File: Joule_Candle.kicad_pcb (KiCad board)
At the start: 2 copper layers, 14 x 80 mm, 7 parts, among them Q1 BC817-40

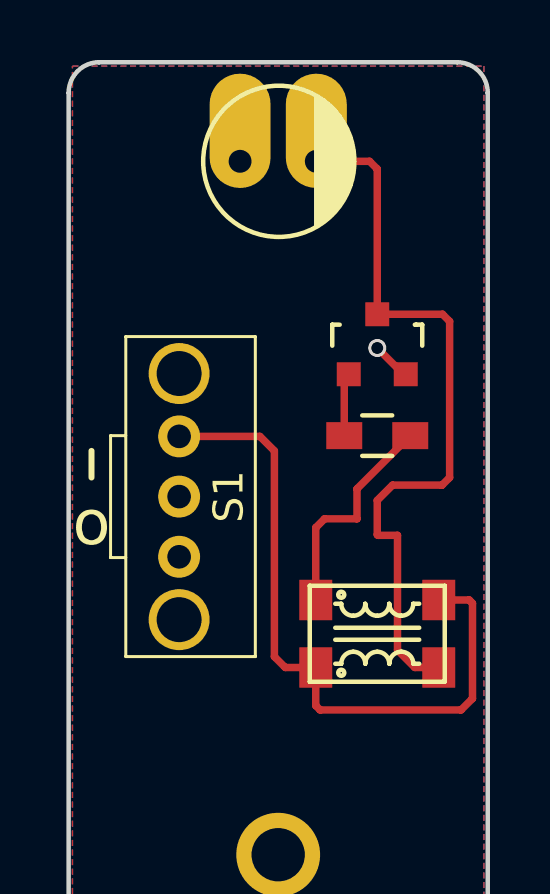
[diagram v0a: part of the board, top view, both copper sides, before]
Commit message: change LED footprint
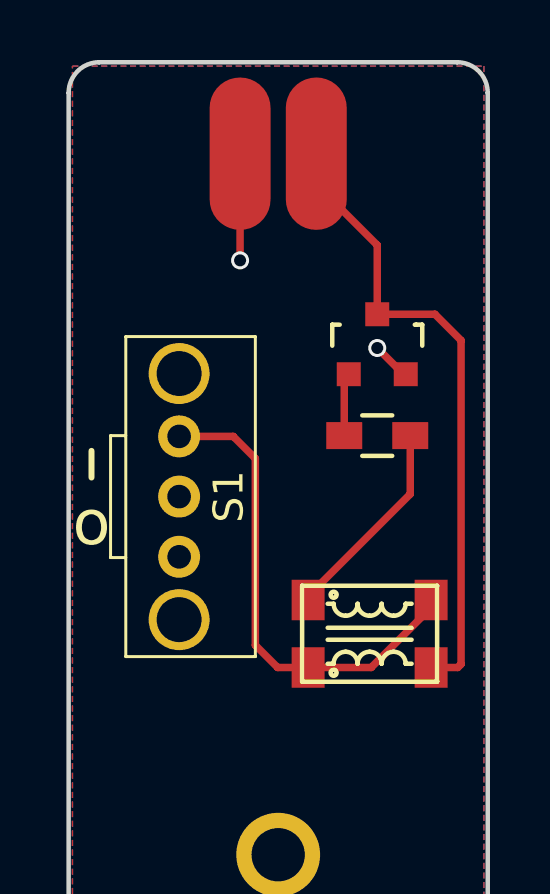
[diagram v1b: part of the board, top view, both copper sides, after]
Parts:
- D1: footprint LEDs:3mm_PCB_Edge -> lib_fp:3mm_PCB_Edge
- moved D1 0.76 mm to (162.3, 55.9)
- moved L1 0.25 mm to (164.1, 70.9)
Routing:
- net Net-(L1-Pad1): track 22.8 -> 16.2 mm
- net Net-(D1-Pad2): track 24.7 -> 20.2 mm
- net GND: track 1.31 -> 3.85 mm, vias 1 -> 2
- net Net-(L1-Pad4): track 7.42 -> 6.89 mm
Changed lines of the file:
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@@
     (thickness 1.6)
     (drawings 61)
-    (tracks 37)
+    (tracks 24)
     (zones 0)
     (modules 7)
@@
       (net 2 GND))
   )
-  (module LEDs:3mm_PCB_Edge (layer F.Cu)
-    (at 162.306 55.118)
-    (fp_text reference D1 (at -1.27 3.302) (layer F.SilkS) hide
-      (effects (font (size 1 1) (thickness 0.15)))
-    )
-    (fp_text value LED (at -1.143 1.397) (layer F.Fab)
-      (effects (font (size 1 1) (thickness 0.15)))
-    )
-    (fp_line (start 1.143 0.762) (end 1.143 -0.762) (layer F.SilkS) (width 0.15))
-    (fp_line (start 1.016 -1.016) (end 1.016 1.016) (layer F.SilkS) (width 0.15))
-    (fp_line (start 0.889 1.27) (end 0.889 -1.27) (layer F.SilkS) (width 0.15))
-    (fp_line (start 0.762 -1.524) (end 0.762 1.397) (layer F.SilkS) (width 0.15))
-    (fp_line (start 0.635 1.651) (end 0.635 -1.651) (layer F.SilkS) (width 0.15))
-    (fp_line (start 0.508 -1.778) (end 0.508 1.778) (layer F.SilkS) (width 0.15))
-    (fp_line (start 0.381 1.905) (end 0.381 -1.905) (layer F.SilkS) (width 0.15))
-    (fp_line (start 0.254 -2.032) (end 0.254 1.905) (layer F.SilkS) (width 0.15))
-    (fp_line (start 0.127 2.032) (end 0.127 -2.032) (layer F.SilkS) (width 0.15))
-    (fp_line (start 0 2.159) (end 0 -2.159) (layer F.SilkS) (width 0.15))
-    (fp_circle (center -1.25 0) (end 1.27 0) (layer F.SilkS) (width 0.15))
-    (pad 1 thru_hole oval (at -2.54 0) (size 2.032 3.81) (drill 0.762 (offset 0 -1.016)) (layers *.Cu *.Mask F.SilkS)
-      (net 2 GND))
-    (pad 2 thru_hole oval (at 0 0) (size 2.032 3.81) (drill 0.762 (offset 0 -1.016)) (layers *.Cu *.Mask F.SilkS)
-      (net 3 "Net-(D1-Pad2)"))
-    (model "../../../../../../home/sam/Dropbox/FreeCAD/Joule Thief/3mmLED.wrl"
-      (at (xyz -0.05 0 0))
-      (scale (xyz 0.3937 0.3937 0.3937))
-      (rotate (xyz 0 0 0))
-    )
-  )
   (module TO_SOT_Packages_SMD:SOT-23 (layer F.Cu)
     (at 164.338 61.214)
@@
   )
   (module Inductor:SRF4532-510Y (layer F.Cu)
-    (at 164.338 70.866)
+    (at 164.084 70.866)
     (fp_text reference L1 (at 0 2.6) (layer F.SilkS) hide
       (effects (font (size 1 1) (thickness 0.15)))
@@
       (xy 2.975 8.625)) (layer F.SilkS) (width 0.01))
   )
+  (module lib_fp:3mm_PCB_Edge (layer F.Cu)
+    (at 162.306 55.88)
+    (fp_text reference D1 (at 0 0) (layer F.SilkS) hide
+      (effects (font (size 1 1) (thickness 0.15)))
+    )
+    (fp_text value LED (at -1.143 1.397) (layer F.Fab)
+      (effects (font (size 1 1) (thickness 0.15)))
+    )
+    (pad 1 smd oval (at -2.54 0) (size 2.032 5.08) (drill (offset 0 -1.016)) (layers F.Cu F.Paste F.Mask)
+      (net 2 GND))
+    (pad 2 smd oval (at 0 0) (size 2.032 5.08) (drill (offset 0 -1.016)) (layers F.Cu F.Paste F.Mask)
+      (net 3 "Net-(D1-Pad2)"))
+    (model "../../../../../../home/sam/Dropbox/FreeCAD/Joule Thief/3mmLED.wrl"
+      (at (xyz -0.05 0 0))
+      (scale (xyz 0.3937 0.3937 0.3937))
+      (rotate (xyz 0 0 0))
+    )
+  )
   (gr_line (start 156.972 126.746) (end 165.1 126.746) (angle 90) (layer B.SilkS) (width 0.2))
   (gr_arc (start 165.1 126.111) (end 165.1 125.476) (angle 90) (layer B.SilkS) (width 0.2))
@@
   (gr_arc (start 167.005 52.832) (end 167.005 51.816) (angle 90) (layer Edge.Cuts) (width 0.15))
   (gr_line (start 154.051 131.826) (end 168.021 131.826) (angle 90) (layer Edge.Cuts) (width 0.15))
+  (segment (start 159.766 55.88) (end 159.766 58.42) (width 0.25) (layer F.Cu) (net 2) (status 400000))
+  (via (at 159.766 58.42) (size 0.6) (drill 0.4) (layers F.Cu B.Cu) (net 2))
   (segment (start 165.288 62.21476) (end 165.21176 62.21476) (width 0.25) (layer F.Cu) (net 2))
   (segment (start 165.21176 62.21476) (end 164.338 61.341) (width 0.25) (layer F.Cu) (net 2))
   (via (at 164.338 61.341) (size 0.6) (drill 0.4) (layers F.Cu B.Cu) (net 2))
-  (segment (start 165.013 67.585) (end 164.359 67.585) (width 0.25) (layer F.Cu) (net 3))
-  (segment (start 166.51478 60.21578) (end 164.338 60.21578) (width 0.25) (layer F.Cu) (net 3))
-  (segment (start 166.751 60.452) (end 166.51478 60.21578) (width 0.25) (layer F.Cu) (net 3))
-  (segment (start 166.751 65.659) (end 166.751 60.452) (width 0.25) (layer F.Cu) (net 3))
-  (segment (start 166.497 65.913) (end 166.751 65.659) (width 0.25) (layer F.Cu) (net 3))
-  (segment (start 164.846 65.913) (end 166.497 65.913) (width 0.25) (layer F.Cu) (net 3))
-  (segment (start 164.338 66.421) (end 164.846 65.913) (width 0.25) (layer F.Cu) (net 3))
-  (segment (start 164.338 67.564) (end 164.338 66.421) (width 0.25) (layer F.Cu) (net 3))
-  (segment (start 164.359 67.585) (end 164.338 67.564) (width 0.25) (layer F.Cu) (net 3))
-  (segment (start 164.338 60.21578) (end 164.338 55.372) (width 0.25) (layer F.Cu) (net 3))
-  (segment (start 164.338 55.372) (end 164.084 55.118) (width 0.25) (layer F.Cu) (net 3))
-  (segment (start 164.084 55.118) (end 162.306 55.118) (width 0.25) (layer F.Cu) (net 3))
-  (segment (start 166.388 71.991) (end 165.59 71.991) (width 0.25) (layer F.Cu) (net 3))
-  (segment (start 165.013 71.414) (end 165.013 67.585) (width 0.25) (layer F.Cu) (net 3))
-  (segment (start 165.59 71.991) (end 165.013 71.414) (width 0.25) (layer F.Cu) (net 3))
-  (segment (start 162.288 71.991) (end 162.288 73.261) (width 0.25) (layer F.Cu) (net 4))
-  (segment (start 167.404 69.741) (end 166.388 69.741) (width 0.25) (layer F.Cu) (net 4))
-  (segment (start 167.513 69.85) (end 167.404 69.741) (width 0.25) (layer F.Cu) (net 4))
-  (segment (start 167.513 73.025) (end 167.513 69.85) (width 0.25) (layer F.Cu) (net 4))
-  (segment (start 167.132 73.406) (end 167.513 73.025) (width 0.25) (layer F.Cu) (net 4))
-  (segment (start 162.433 73.406) (end 167.132 73.406) (width 0.25) (layer F.Cu) (net 4))
-  (segment (start 162.288 73.261) (end 162.433 73.406) (width 0.25) (layer F.Cu) (net 4))
-  (segment (start 157.734 64.2874) (end 160.4264 64.2874) (width 0.25) (layer F.Cu) (net 4))
-  (segment (start 161.272 71.991) (end 162.288 71.991) (width 0.25) (layer F.Cu) (net 4))
-  (segment (start 160.909 71.628) (end 161.272 71.991) (width 0.25) (layer F.Cu) (net 4))
-  (segment (start 160.909 64.77) (end 160.909 71.628) (width 0.25) (layer F.Cu) (net 4))
-  (segment (start 160.4264 64.2874) (end 160.909 64.77) (width 0.25) (layer F.Cu) (net 4))
+  (segment (start 166.134 71.991) (end 167.023 71.991) (width 0.25) (layer F.Cu) (net 3) (status 400000))
+  (segment (start 166.26078 60.21578) (end 164.338 60.21578) (width 0.25) (layer F.Cu) (net 3) (status 800000))
+  (segment (start 167.132 61.087) (end 166.26078 60.21578) (width 0.25) (layer F.Cu) (net 3))
+  (segment (start 167.132 71.882) (end 167.132 61.087) (width 0.25) (layer F.Cu) (net 3))
+  (segment (start 167.023 71.991) (end 167.132 71.882) (width 0.25) (layer F.Cu) (net 3))
+  (segment (start 164.338 60.21578) (end 164.338 57.912) (width 0.25) (layer F.Cu) (net 3))
+  (segment (start 164.338 57.912) (end 162.306 55.88) (width 0.25) (layer F.Cu) (net 3))
+  (segment (start 157.734 64.2874) (end 159.5374 64.2874) (width 0.25) (layer F.Cu) (net 4) (status 400000))
+  (segment (start 161.018 71.991) (end 162.034 71.991) (width 0.25) (layer F.Cu) (net 4) (status 800000))
+  (segment (start 160.274 71.247) (end 161.018 71.991) (width 0.25) (layer F.Cu) (net 4))
+  (segment (start 160.274 65.024) (end 160.274 71.247) (width 0.25) (layer F.Cu) (net 4))
+  (segment (start 159.5374 64.2874) (end 160.274 65.024) (width 0.25) (layer F.Cu) (net 4))
+  (segment (start 162.288 71.991) (end 164.138 71.991) (width 0.25) (layer F.Cu) (net 4))
+  (segment (start 164.138 71.991) (end 166.388 69.741) (width 0.25) (layer F.Cu) (net 4))
   (segment (start 163.238 64.262) (end 163.238 62.36476) (width 0.25) (layer F.Cu) (net 6))
   (segment (start 163.238 62.36476) (end 163.388 62.21476) (width 0.25) (layer F.Cu) (net 6))
-  (segment (start 163.663 67.035) (end 163.663 66.037) (width 0.25) (layer F.Cu) (net 7))
-  (segment (start 163.663 66.037) (end 165.438 64.262) (width 0.25) (layer F.Cu) (net 7))
-  (segment (start 162.288 69.741) (end 162.288 67.328) (width 0.25) (layer F.Cu) (net 7))
-  (segment (start 162.581 67.035) (end 163.663 67.035) (width 0.25) (layer F.Cu) (net 7))
-  (segment (start 162.288 67.328) (end 162.581 67.035) (width 0.25) (layer F.Cu) (net 7))
+  (segment (start 162.034 69.741) (end 162.034 69.614) (width 0.25) (layer F.Cu) (net 7) (status C00000))
+  (segment (start 162.034 69.614) (end 165.438 66.21) (width 0.25) (layer F.Cu) (net 7) (status 400000))
+  (segment (start 165.438 66.21) (end 165.438 64.262) (width 0.25) (layer F.Cu) (net 7) (status 800000))
   (zone (net 2) (net_name GND) (layer B.Cu) (hatch edge 0.508)
     (connect_pads (clearance 0.508))

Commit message: remove 3d shapes
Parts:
- moved LOGO 2.07 mm to (159.8, 91.4)
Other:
- board text added: "Joule Thief Candle V2"
- board text added: "Sam Perry October 2017"
- board text removed: "Joule Thief Candle"
- board text removed: "Sam Perry November 2016"
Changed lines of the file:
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@@
     (links 11)
     (no_connects 0)
-    (area 152.949 51.740999 170.323715 131.901001)
+    (area 153.975999 51.740999 168.096001 131.901001)
     (thickness 1.6)
-    (drawings 61)
+    (drawings 36)
     (tracks 24)
     (zones 0)
@@
     (36 B.SilkS user)
     (37 F.SilkS user)
-    (38 B.Mask user hide)
-    (39 F.Mask user hide)
+    (38 B.Mask user)
+    (39 F.Mask user)
     (40 Dwgs.User user hide)
     (41 Cmts.User user hide)
@@
     (43 Eco2.User user hide)
     (44 Edge.Cuts user)
-    (45 Margin user hide)
+    (45 Margin user)
     (46 B.CrtYd user hide)
     (47 F.CrtYd user hide)
@@
     (pad 3 smd rect (at 0 -0.99822) (size 0.8001 0.8001) (layers F.Cu F.Paste F.Mask)
       (net 3 "Net-(D1-Pad2)"))
-    (model TO_SOT_Packages_SMD.3dshapes/SOT-23.wrl
-      (at (xyz 0 0 0))
-      (scale (xyz 1 1 1))
-      (rotate (xyz 0 0 0))
-    )
   )
   (module Resistors_SMD:R_0603_HandSoldering (layer F.Cu)
@@
     (pad 2 smd rect (at 1.1 0 180) (size 1.2 0.9) (layers F.Cu F.Paste F.Mask)
       (net 6 "Net-(Q1-Pad1)"))
-    (model Resistors_SMD.3dshapes/R_0603_HandSoldering.wrl
-      (at (xyz 0 0 0))
-      (scale (xyz 1 1 1))
-      (rotate (xyz 0 0 0))
-    )
   )
   (module Switches:SPDT_OS102011MA1QN1 (layer F.Cu)
@@
     (pad "" thru_hole circle (at -4.1021 0 90) (size 2.032 2.032) (drill 1.4986) (layers *.Cu *.Mask F.SilkS))
     (pad "" thru_hole circle (at 4.1021 0 90) (size 2.032 2.032) (drill 1.4986) (layers *.Cu *.Mask F.SilkS))
-    (model "../../../../../../home/sam/Dropbox/FreeCAD/AVR Dragon Shield/SPDT_Switch.wrl"
-      (at (xyz 0 0 0))
-      (scale (xyz 0.393701 0.393701 0.393701))
-      (rotate (xyz 0 0 180))
-    )
   )
   (module Inductor:SRF4532-510Y (layer F.Cu)
@@
   )
   (module Logo:P-Logo_Small (layer F.Cu)
-    (at 157.734 91.821)
+    (at 159.766 91.44)
     (fp_text reference LOGO (at 0 5) (layer F.SilkS) hide
       (effects (font (thickness 0.3)))
@@
     (pad 2 smd oval (at 0 0) (size 2.032 5.08) (drill (offset 0 -1.016)) (layers F.Cu F.Paste F.Mask)
       (net 3 "Net-(D1-Pad2)"))
-    (model "../../../../../../home/sam/Dropbox/FreeCAD/Joule Thief/3mmLED.wrl"
-      (at (xyz -0.05 0 0))
-      (scale (xyz 0.3937 0.3937 0.3937))
-      (rotate (xyz 0 0 0))
-    )
   )
-  (gr_line (start 156.972 126.746) (end 165.1 126.746) (angle 90) (layer B.SilkS) (width 0.2))
-  (gr_arc (start 165.1 126.111) (end 165.1 125.476) (angle 90) (layer B.SilkS) (width 0.2))
-  (gr_arc (start 156.972 126.111) (end 156.972 126.746) (angle 90) (layer B.SilkS) (width 0.2))
-  (gr_arc (start 165.1 126.111) (end 165.735 126.111) (angle 90) (layer B.SilkS) (width 0.2))
-  (gr_arc (start 156.972 126.111) (end 156.337 126.111) (angle 90) (layer B.SilkS) (width 0.2))
-  (gr_line (start 159.258 130.429) (end 159.639 127.254) (angle 90) (layer B.SilkS) (width 0.2))
-  (gr_line (start 162.814 130.429) (end 162.433 127.254) (angle 90) (layer B.SilkS) (width 0.2))
-  (gr_arc (start 163.195 130.429) (end 163.195 130.81) (angle 90) (layer B.SilkS) (width 0.2))
-  (gr_arc (start 158.877 130.429) (end 159.258 130.429) (angle 90) (layer B.SilkS) (width 0.2))
-  (gr_line (start 155.067 130.937) (end 155.067 131.191) (angle 90) (layer B.SilkS) (width 0.2))
-  (gr_line (start 167.005 130.937) (end 167.005 131.191) (angle 90) (layer B.SilkS) (width 0.2))
-  (gr_line (start 166.878 130.81) (end 155.194 130.81) (angle 90) (layer B.SilkS) (width 0.2))
-  (gr_arc (start 166.878 130.937) (end 166.878 130.81) (angle 90) (layer B.SilkS) (width 0.2))
-  (gr_arc (start 155.194 130.937) (end 155.067 130.937) (angle 90) (layer B.SilkS) (width 0.2))
-  (gr_line (start 154.813 131.191) (end 167.259 131.191) (angle 90) (layer B.SilkS) (width 0.2))
-  (gr_line (start 165.481 125.476) (end 156.591 125.476) (angle 90) (layer B.SilkS) (width 0.2))
-  (gr_line (start 155.575 124.46) (end 166.497 124.46) (angle 90) (layer B.SilkS) (width 0.2))
-  (gr_arc (start 154.813 131.699) (end 154.305 131.699) (angle 90) (layer B.SilkS) (width 0.2))
-  (gr_arc (start 167.259 131.699) (end 167.259 131.191) (angle 90) (layer B.SilkS) (width 0.2))
-  (gr_line (start 154.305 131.699) (end 167.767 131.699) (angle 90) (layer B.SilkS) (width 0.2))
-  (gr_line (start 155.575 124.46) (end 156.591 125.476) (angle 90) (layer B.SilkS) (width 0.2))
-  (gr_line (start 166.497 124.46) (end 165.481 125.476) (angle 90) (layer B.SilkS) (width 0.2))
-  (gr_arc (start 155.575 123.19) (end 155.575 124.46) (angle 90) (layer B.SilkS) (width 0.2))
-  (gr_arc (start 166.497 123.19) (end 167.767 123.19) (angle 90) (layer B.SilkS) (width 0.2))
-  (gr_line (start 154.305 123.19) (end 167.767 123.19) (angle 90) (layer B.SilkS) (width 0.2))
   (gr_line (start 161.29 57.15) (end 161.29 56.388) (angle 90) (layer B.SilkS) (width 0.2))
   (gr_line (start 161.036 57.15) (end 161.036 56.261) (angle 90) (layer B.SilkS) (width 0.2))
@@
   (gr_arc (start 161.798 60.325) (end 162.306 60.325) (angle 90) (layer B.SilkS) (width 0.2))
   (gr_arc (start 161.798 60.325) (end 161.798 60.833) (angle 90) (layer B.SilkS) (width 0.2))
-  (gr_text "Joule Thief \nCandle" (at 158.369 106.426 90) (layer F.SilkS)
+  (gr_text "Joule Thief Candle V2" (at 156.845 103.124 90) (layer F.SilkS)
     (effects (font (size 1.5 1.5) (thickness 0.3)))
   )
@@
     (effects (font (size 1.5 1.5) (thickness 0.3)))
   )
-  (gr_text "Sam Perry\nNovember 2016" (at 165.1 128.778 90) (layer F.Mask)
+  (gr_text "Sam Perry\nOctober 2017" (at 165.1 128.778 90) (layer F.Mask)
     (effects (font (size 1.016 1.016) (thickness 0.254)) (justify left))
   )
@@
   (gr_arc (start 167.005 52.832) (end 167.005 51.816) (angle 90) (layer Edge.Cuts) (width 0.15))
   (gr_line (start 154.051 131.826) (end 168.021 131.826) (angle 90) (layer Edge.Cuts) (width 0.15))
-  (segment (start 159.766 55.88) (end 159.766 58.42) (width 0.25) (layer F.Cu) (net 2) (status 400000))
+  (segment (start 159.766 55.88) (end 159.766 58.42) (width 0.25) (layer F.Cu) (net 2))
   (via (at 159.766 58.42) (size 0.6) (drill 0.4) (layers F.Cu B.Cu) (net 2))
   (segment (start 165.288 62.21476) (end 165.21176 62.21476) (width 0.25) (layer F.Cu) (net 2))
   (segment (start 165.21176 62.21476) (end 164.338 61.341) (width 0.25) (layer F.Cu) (net 2))
   (via (at 164.338 61.341) (size 0.6) (drill 0.4) (layers F.Cu B.Cu) (net 2))
-  (segment (start 166.134 71.991) (end 167.023 71.991) (width 0.25) (layer F.Cu) (net 3) (status 400000))
-  (segment (start 166.26078 60.21578) (end 164.338 60.21578) (width 0.25) (layer F.Cu) (net 3) (status 800000))
+  (segment (start 166.134 71.991) (end 167.023 71.991) (width 0.25) (layer F.Cu) (net 3))
+  (segment (start 166.26078 60.21578) (end 164.338 60.21578) (width 0.25) (layer F.Cu) (net 3))
   (segment (start 167.132 61.087) (end 166.26078 60.21578) (width 0.25) (layer F.Cu) (net 3))
   (segment (start 167.132 71.882) (end 167.132 61.087) (width 0.25) (layer F.Cu) (net 3))
@@
   (segment (start 164.338 60.21578) (end 164.338 57.912) (width 0.25) (layer F.Cu) (net 3))
   (segment (start 164.338 57.912) (end 162.306 55.88) (width 0.25) (layer F.Cu) (net 3))
-  (segment (start 157.734 64.2874) (end 159.5374 64.2874) (width 0.25) (layer F.Cu) (net 4) (status 400000))
-  (segment (start 161.018 71.991) (end 162.034 71.991) (width 0.25) (layer F.Cu) (net 4) (status 800000))
+  (segment (start 157.734 64.2874) (end 159.5374 64.2874) (width 0.25) (layer F.Cu) (net 4))
+  (segment (start 161.018 71.991) (end 162.034 71.991) (width 0.25) (layer F.Cu) (net 4))
   (segment (start 160.274 71.247) (end 161.018 71.991) (width 0.25) (layer F.Cu) (net 4))
   (segment (start 160.274 65.024) (end 160.274 71.247) (width 0.25) (layer F.Cu) (net 4))
@@
   (segment (start 163.238 64.262) (end 163.238 62.36476) (width 0.25) (layer F.Cu) (net 6))
   (segment (start 163.238 62.36476) (end 163.388 62.21476) (width 0.25) (layer F.Cu) (net 6))
-  (segment (start 162.034 69.741) (end 162.034 69.614) (width 0.25) (layer F.Cu) (net 7) (status C00000))
-  (segment (start 162.034 69.614) (end 165.438 66.21) (width 0.25) (layer F.Cu) (net 7) (status 400000))
-  (segment (start 165.438 66.21) (end 165.438 64.262) (width 0.25) (layer F.Cu) (net 7) (status 800000))
+  (segment (start 162.034 69.741) (end 162.034 69.614) (width 0.25) (layer F.Cu) (net 7))
+  (segment (start 162.034 69.614) (end 165.438 66.21) (width 0.25) (layer F.Cu) (net 7))
+  (segment (start 165.438 66.21) (end 165.438 64.262) (width 0.25) (layer F.Cu) (net 7))
   (zone (net 2) (net_name GND) (layer B.Cu) (hatch edge 0.508)
     (connect_pads (clearance 0.508))

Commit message: update silkscreen
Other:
- board text added: "+"
- board text added: "Joule Thief Candle V1.1"
- board text added: "ON"
- board text removed: "Joule Thief Candle V2"
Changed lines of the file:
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@@
     (area 153.975999 51.740999 168.096001 131.901001)
     (thickness 1.6)
-    (drawings 36)
+    (drawings 38)
     (tracks 24)
     (zones 0)
@@
       (net 3 "Net-(D1-Pad2)"))
   )
+  (gr_text + (at 164.338 54.864) (layer F.SilkS)
+    (effects (font (size 1.5 1.5) (thickness 0.3)))
+  )
+  (gr_text ON (at 155.702 59.436) (layer F.SilkS)
+    (effects (font (size 1.5 1.5) (thickness 0.3)))
+  )
   (gr_line (start 161.29 57.15) (end 161.29 56.388) (angle 90) (layer B.SilkS) (width 0.2))
   (gr_line (start 161.036 57.15) (end 161.036 56.261) (angle 90) (layer B.SilkS) (width 0.2))
@@
   (gr_arc (start 161.798 60.325) (end 162.306 60.325) (angle 90) (layer B.SilkS) (width 0.2))
   (gr_arc (start 161.798 60.325) (end 161.798 60.833) (angle 90) (layer B.SilkS) (width 0.2))
-  (gr_text "Joule Thief Candle V2" (at 156.845 103.124 90) (layer F.SilkS)
+  (gr_text "Joule Thief Candle\nV1.1" (at 157.734 103.124 90) (layer F.SilkS)
     (effects (font (size 1.5 1.5) (thickness 0.3)))
   )
